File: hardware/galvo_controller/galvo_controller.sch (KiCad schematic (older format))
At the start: 116 parts, among them J1 USB_OTG, J2 Conn_01x03, J3 Conn_01x03, J4 Micro_SD_Card, J5 Red, J6 White, J7 Conn_01x03, J8 Conn_01x03, Q1 DDTD113ZC, Q2 MMBT2222, Q3 MMBT2222, U1 ESP-WROOM-32D, U2 CP2104, U3 TPS54295PWP, U4 PCM3060, U5 NCP1117LP, U6 OPA2134, U7 LME49724, U8 LME49724

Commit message: Working on schematic
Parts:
- J5, J6: footprint (none) -> footprint:RCJ-01x
- Q2, Q3: footprint (none) -> TO_SOT_Packages_SMD:SOT-23; Part (none) -> MMBT2222ALT3GOSCT-ND; Source (none) -> DigiKey
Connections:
- net labels added: LASER
- net labels removed: LASER_EN

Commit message: Working on footprints
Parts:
- L1, L2: footprint (none) -> footprint:CLF7045-D
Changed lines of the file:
@@
 F 0 "L2" V 6700 1700 50  0000 C CNN
 F 1 "2.2u" V 6825 1700 50  0000 C CNN
-F 2 "" H 6750 1700 50  0001 C CNN
+F 2 "footprint:CLF7045-D" H 6750 1700 50  0001 C CNN
 F 3 "" H 6750 1700 50  0001 C CNN
 F 4 "DigiKey" H 6750 1700 60  0001 C CNN "Source"
@@
 F 0 "L1" V 4400 1700 50  0000 C CNN
 F 1 "3.3u" V 4525 1700 50  0000 C CNN
-F 2 "" H 4450 1700 50  0001 C CNN
+F 2 "footprint:CLF7045-D" H 4450 1700 50  0001 C CNN
 F 3 "" H 4450 1700 50  0001 C CNN
 F 4 "DigiKey" H 4450 1700 60  0001 C CNN "Source"

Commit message: Working on footprints
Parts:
- removed J4: Micro_SD_Card, symbol Micro_SD_Card
- added J4: Micro_SD_Card_Det, footprint:503182-1853, symbol Micro_SD_Card_Det
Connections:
- wire segments 399 -> 400
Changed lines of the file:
@@
-$EndComp
-$Comp
-L Micro_SD_Card J4
-U 1 1 5AA9BDBD
-P 10500 9100
-F 0 "J4" H 9850 9700 50  0000 C CNN
-F 1 "Micro_SD_Card" H 11150 9700 50  0000 R CNN
-F 2 "" H 11650 9400 50  0001 C CNN
-F 3 "" H 10500 9100 50  0001 C CNN
-	1    10500 9100
-	1    0    0    -1
 $EndComp
 $Comp
@@
 L GNDD #PWR43
 U 1 1 5AA746B2
-P 9500 9600
-F 0 "#PWR43" H 9500 9350 50  0001 C CNN
-F 1 "GNDD" H 9500 9475 50  0000 C CNN
-F 2 "" H 9500 9600 50  0001 C CNN
-F 3 "" H 9500 9600 50  0001 C CNN
-	1    9500 9600
+P 9500 9800
+F 0 "#PWR43" H 9500 9550 50  0001 C CNN
+F 1 "GNDD" H 9500 9675 50  0000 C CNN
+F 2 "" H 9500 9800 50  0001 C CNN
+F 3 "" H 9500 9800 50  0001 C CNN
+	1    9500 9800
 	1    0    0    -1
 $EndComp
@@
 	9600 9300 9500 9300
 Wire Wire Line
-	9500 9300 9500 9600
+	9500 9300 9500 9800
 $Comp
 L +3.3V #PWR42
@@
 Wire Wire Line
 	8700 8050 8700 8100
+$Comp
+L Micro_SD_Card_Det J4
+U 1 1 5AA55079
+P 10500 9200
+F 0 "J4" H 9850 9900 50  0000 C CNN
+F 1 "Micro_SD_Card_Det" H 11150 9900 50  0000 R CNN
+F 2 "footprint:503182-1853" H 12550 9900 50  0001 C CNN
+F 3 "" H 10500 9300 50  0001 C CNN
+F 4 "DigiKey" H 10500 9200 60  0001 C CNN "Source"
+F 5 "WM9750CT-ND" H 10500 9200 60  0001 C CNN "Part"
+	1    10500 9200
+	1    0    0    -1
+$EndComp
+Wire Wire Line
+	9600 9700 9500 9700
+Connection ~ 9500 9700
 $EndSCHEMATC

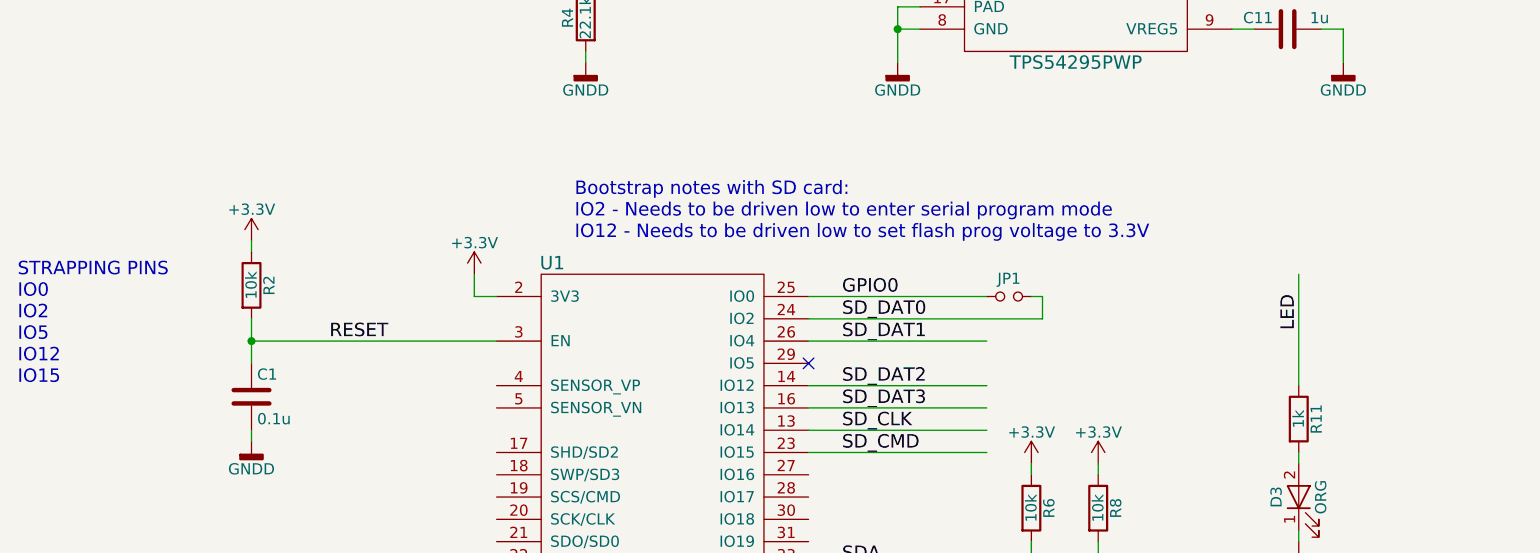
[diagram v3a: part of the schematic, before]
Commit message: Finished BOM, exported to layout
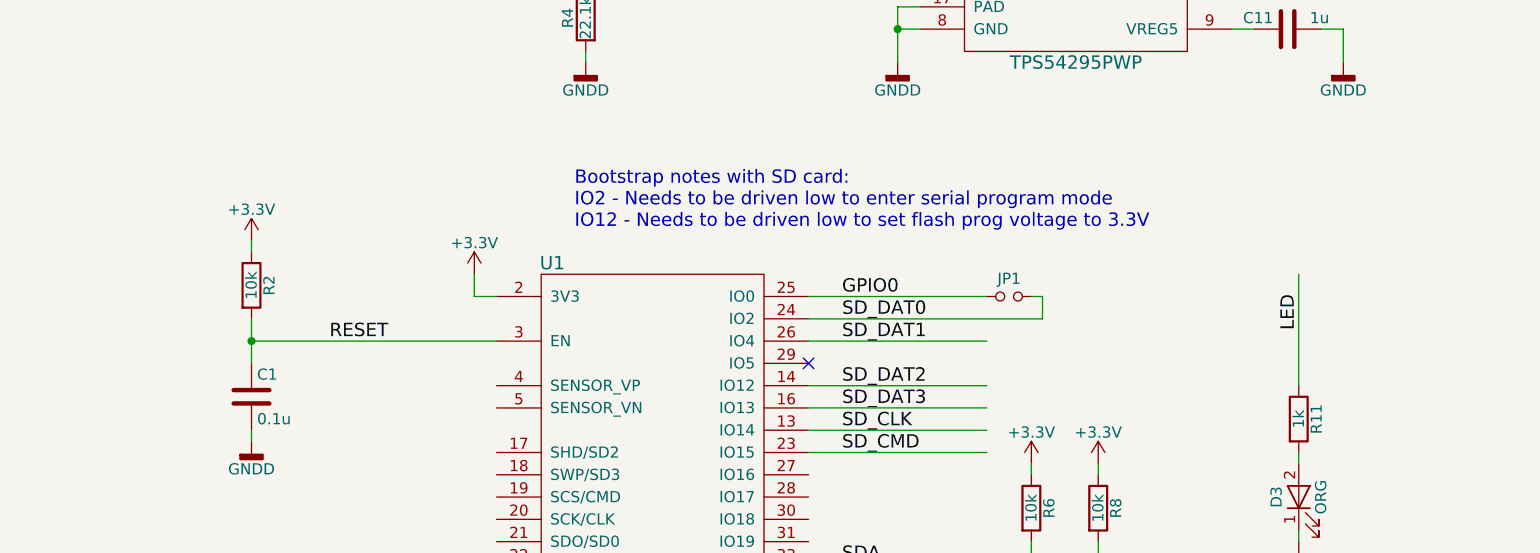
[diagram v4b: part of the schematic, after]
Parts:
- C10, C7: footprint (none) -> Capacitors_SMD:C_0603; Part (none) -> 490-9734-1-ND; Source (none) -> DigiKey
- C11: footprint (none) -> Capacitors_SMD:C_0805; Part (none) -> 490-1691-1-ND; Source (none) -> DigiKey
- C13, C14, C4, C5: Part 311-1995-1-ND -> 490-6509-1-ND
- C28, C29, C30, C31, C32, C33: footprint (none) -> Capacitors_SMD:C_0603; Part (none) -> 490-11460-1-ND; Source (none) -> DigiKey
- C3: footprint (none) -> Capacitors_SMD:C_0805; Part (none) -> 490-5422-1-ND; Source (none) -> DigiKey
- JP1, JP2: Part (none) -> 3M9457-02-ND
- R1: Part (none) -> 311-2.20KHRCT-ND; Source (none) -> DigiKey
- R10, R14, R15, R16, R17, R18, R19, R2, R26, R27, R28, R29, R30, R31, R6, R8, R9: Part (none) -> 311-10.0KHRCT-ND; Source (none) -> DigiKey
- R11, R20, R21, R5, R7: Part (none) -> 311-1.00KHRCT-ND; Source (none) -> DigiKey
- R12: Part (none) -> 311-73.2KHRCT-ND; Source (none) -> DigiKey
- R13, R4: Part (none) -> 311-22.1KHRCT-ND; Source (none) -> DigiKey
- R22, R23, R24, R25: Part (none) -> 311-8.06KHRCT-ND; Source (none) -> DigiKey
- R3: Part (none) -> 311-124KHRCT-ND; Source (none) -> DigiKey
- R32, R33: Part (none) -> 311-20.0KHRCT-ND; Source (none) -> DigiKey
- R34, R35, R36, R37: Part (none) -> 311-0.0GRCT-ND; Source (none) -> DigiKey
- R38, R39: Part (none) -> 311-47.0KHRCT-ND; Source (none) -> DigiKey
- U1: Part (none) -> 1528-1801-ND; Source eBay -> DigiKey
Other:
- note removed: "STRAPPING PINS\nIO0\nIO2\nIO5\nIO12\nIO15"

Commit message: Working on layout
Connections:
- net labels added: D_N, D_P, VBUS, VOUTL_N, VOUTL_P, VOUTR_N, VOUTR_P, X_N, X_P, Y_N, Y_P
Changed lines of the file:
@@
 	9600 9700 9500 9700
 Connection ~ 9500 9700
+Text Label 10100 6550 0    60   ~ 0
+VOUTR_N
+Text Label 10100 6750 0    60   ~ 0
+VOUTR_P
+Text Label 10100 6950 0    60   ~ 0
+VOUTL_N
+Text Label 10100 7150 0    60   ~ 0
+VOUTL_P
+Text Label 14600 5750 0    60   ~ 0
+X_P
+Text Label 14600 5850 0    60   ~ 0
+X_N
+Text Label 14600 7850 0    60   ~ 0
+Y_P
+Text Label 14600 7950 0    60   ~ 0
+Y_N
+Text Label 2150 9000 0    60   ~ 0
+D_N
+Text Label 2150 8900 0    60   ~ 0
+D_P
+Text Label 2150 8800 0    60   ~ 0
+VBUS
 $EndSCHEMATC

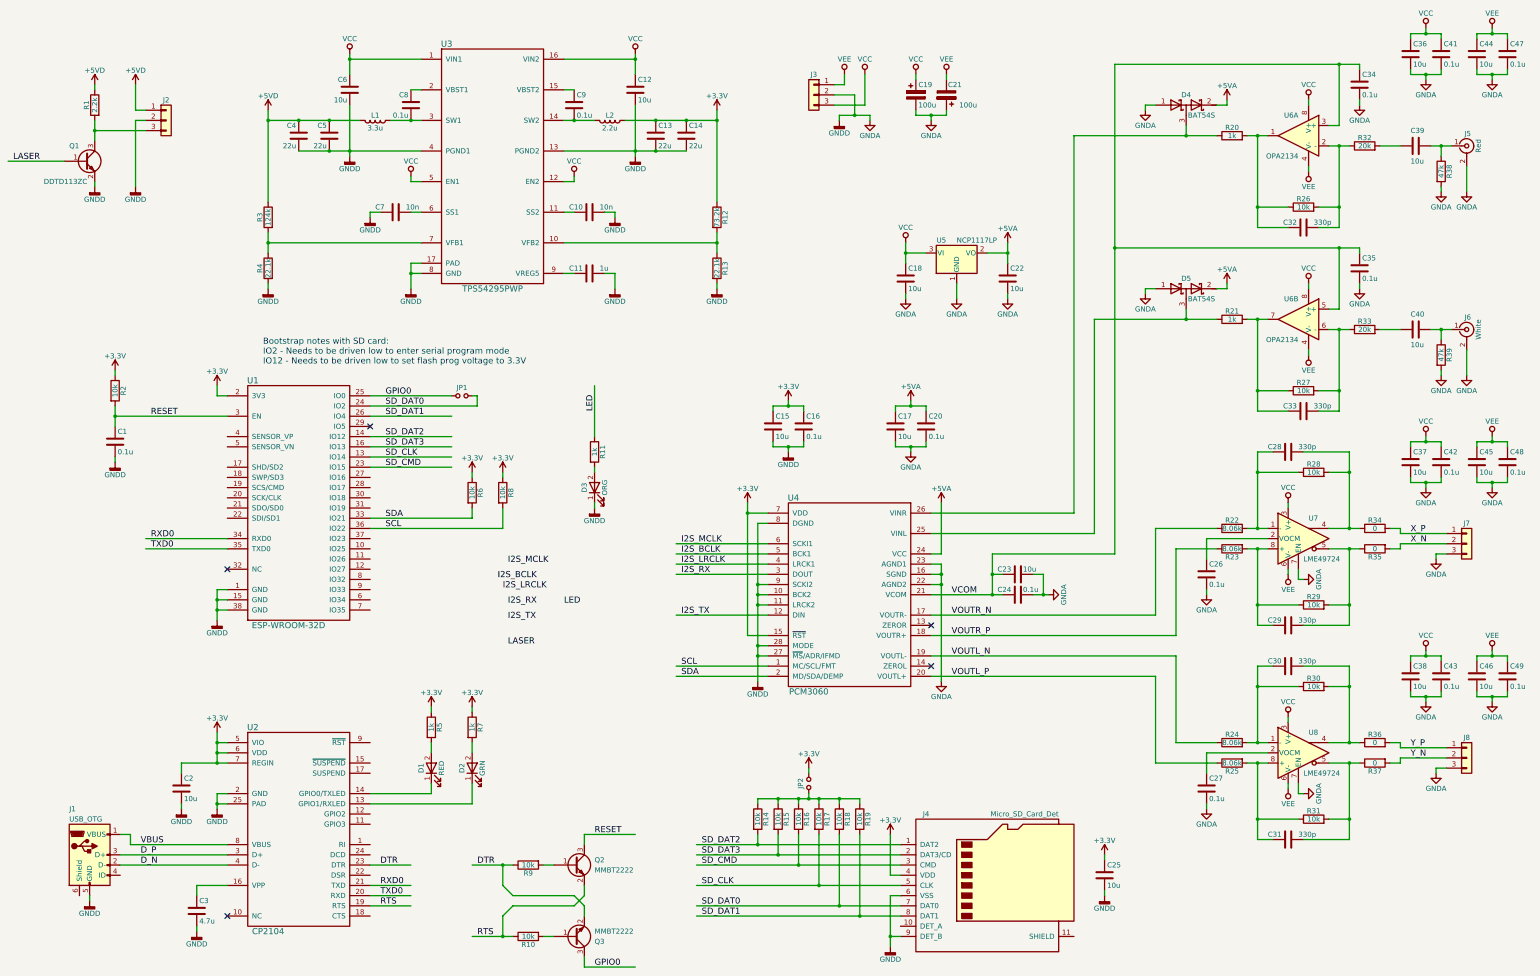
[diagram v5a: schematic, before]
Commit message: Switched to logic buffer for laser enable
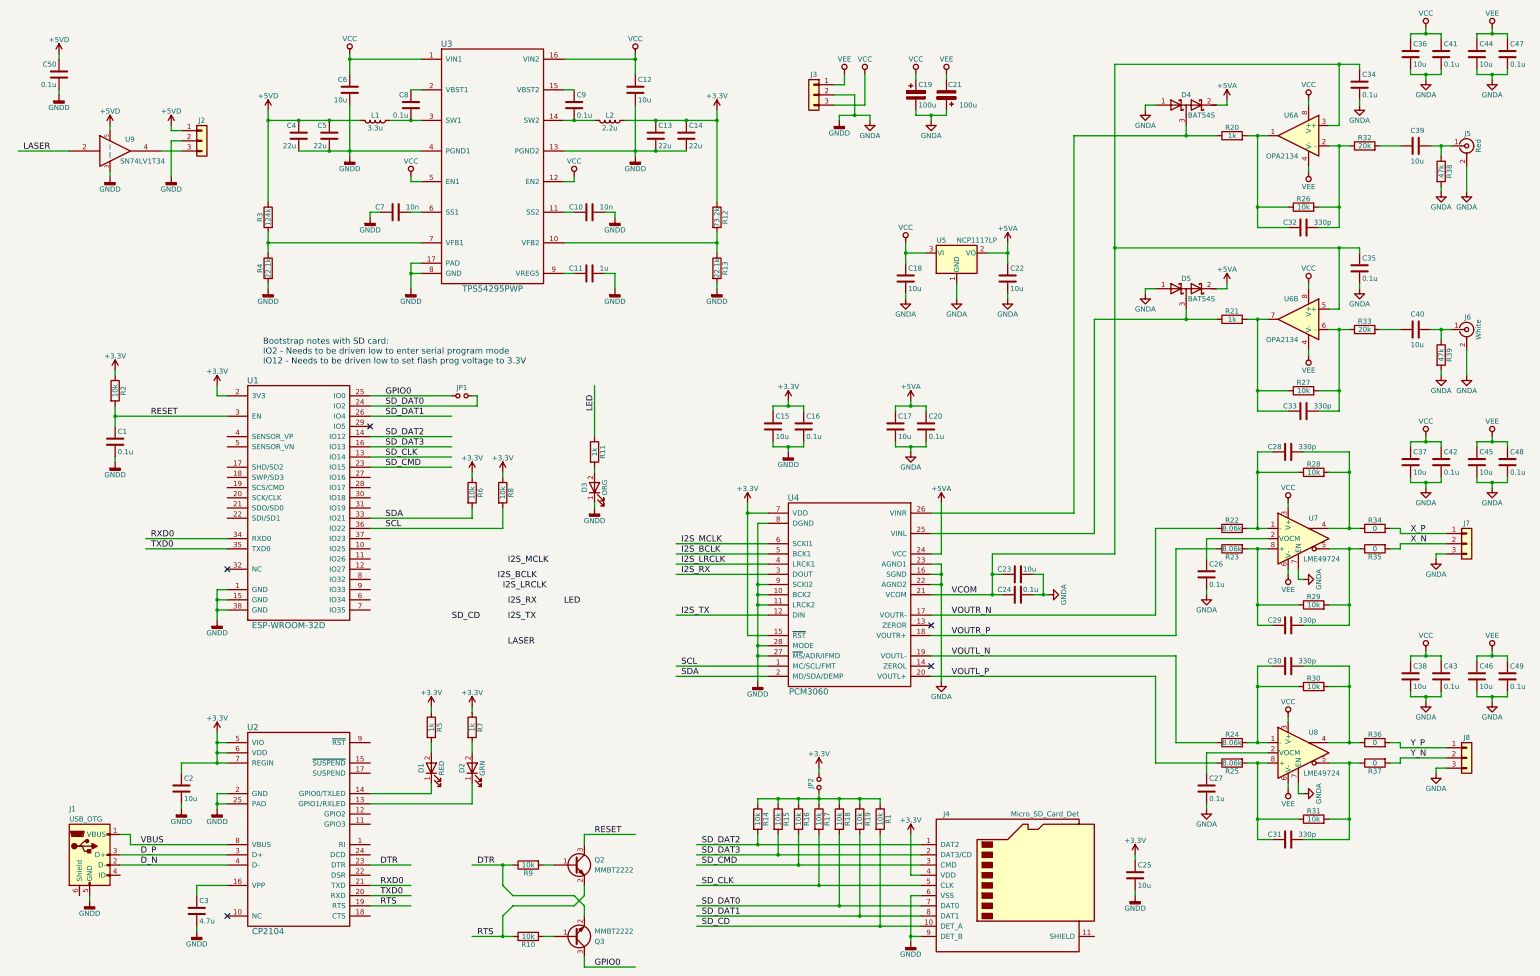
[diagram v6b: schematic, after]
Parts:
- removed Q1: DDTD113ZC, TO_SOT_Packages_SMD:SOT-23, symbol Q_NPN_BEC
- added C50: 0.1u, Capacitors_SMD:C_0603, symbol C
- added U9: SN74LV1T34, TO_SOT_Packages_SMD:SOT-23-5, symbol SN74LV1T34
- R1: value 2.2k -> 10k; Part 311-2.20KHRCT-ND -> 311-10.0KHRCT-ND
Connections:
- net labels added: SD_CD
- wire segments 400 -> 403
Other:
- moved on the sheet: C25, J2, J4, JP2

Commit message: Working on layout
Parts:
- renumbered C50 to C1, C9 to C10, C10 to C11, C11 to C12, C12 to C13, C13 to C14, C14 to C15, C15 to C16, C16 to C17, C17 to C18, C18 to C19, C1 to C2, C19 to C20, C20 to C21, C21 to C22, C22 to C23, C23 to C24, C24 to C25, C25 to C26, C26 to C27, C27 to C28, C28 to C29, C2 to C3, C29 to C30, C30 to C31, C31 to C32, C32 to C33, C33 to C34, C34 to C35, C35 to C36, C36 to C37, C37 to C38, C38 to C39, C3 to C4, C39 to C40, C40 to C41, C41 to C42, C42 to C43, C43 to C44, C44 to C45, C45 to C46, C46 to C47, C47 to C48, C48 to C49, C4 to C5, C49 to C50, C5 to C6, C6 to C7, C7 to C8, C8 to C9, Q2 to Q1, Q3 to Q2, R2 to R1, R11 to R10, R12 to R11, R13 to R12, R14 to R13, R15 to R14, R16 to R15, R17 to R16, R18 to R17, R19 to R18, R1 to R19, R3 to R2, R4 to R3, R5 to R4, R6 to R5, R7 to R6, R8 to R7, R9 to R8, R10 to R9, U9 to U1, U1 to U2, U2 to U3, U3 to U4, U4 to U5, U5 to U6, U6 to U7, U7 to U8, U8 to U9

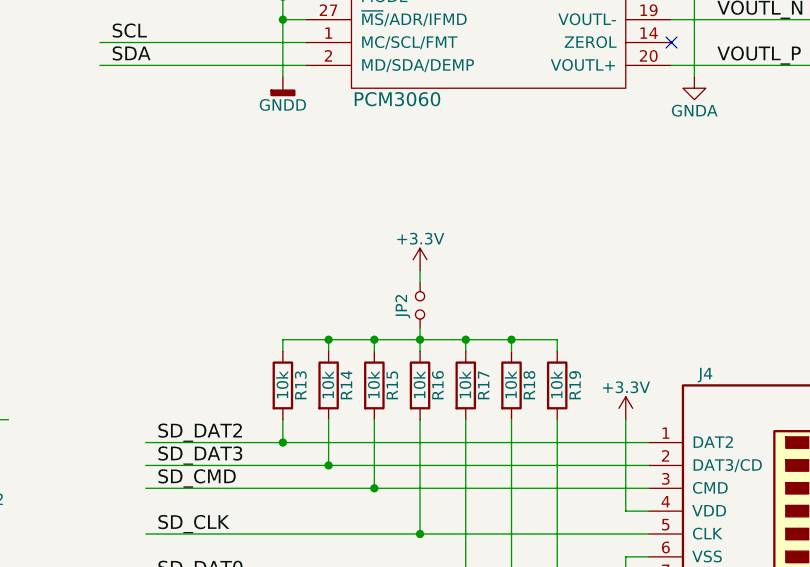
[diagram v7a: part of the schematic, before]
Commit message: Tweaked SD card pullup jumpers
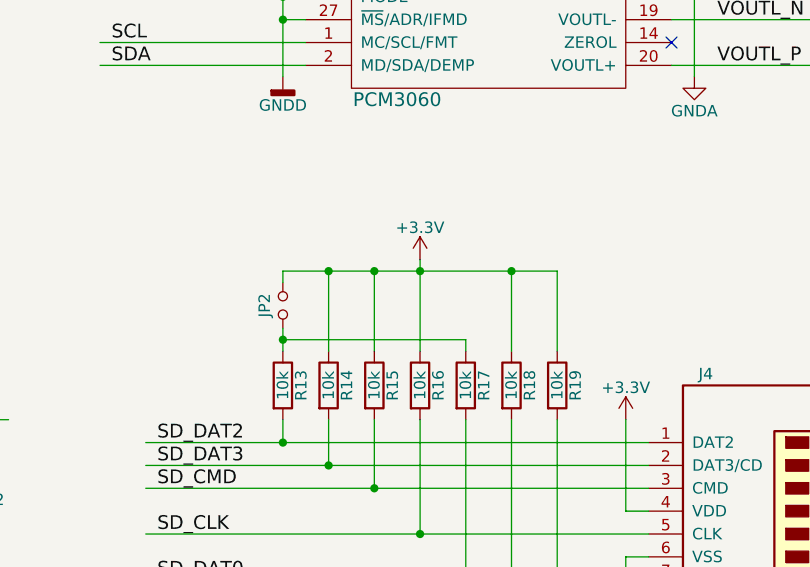
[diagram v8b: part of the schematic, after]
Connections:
- wire segments 403 -> 404
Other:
- moved on the sheet: JP2
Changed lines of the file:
@@
 L +3.3V #PWR39
 U 1 1 5AA8914A
-P 8800 8050
-F 0 "#PWR39" H 8800 7900 50  0001 C CNN
-F 1 "+3.3V" H 8800 8190 50  0000 C CNN
-F 2 "" H 8800 8050 50  0001 C CNN
-F 3 "" H 8800 8050 50  0001 C CNN
-	1    8800 8050
+P 8800 8000
+F 0 "#PWR39" H 8800 7850 50  0001 C CNN
+F 1 "+3.3V" H 8800 8140 50  0000 C CNN
+F 2 "" H 8800 8000 50  0001 C CNN
+F 3 "" H 8800 8000 50  0001 C CNN
+	1    8800 8000
 	1    0    0    -1
 $EndComp
@@
 L Jumper_NO_Small JP2
 U 1 1 5AA977C1
-P 8800 8200
-F 0 "JP2" H 8800 8280 50  0000 C CNN
-F 1 "Jumper_NO_Small" H 8810 8140 50  0001 C CNN
-F 2 "Pin_Headers:Pin_Header_Straight_1x02_Pitch2.54mm" H 8800 8200 50  0001 C CNN
-F 3 "" H 8800 8200 50  0001 C CNN
-F 4 "DigiKey" H 8800 8200 60  0001 C CNN "Source"
-F 5 "3M9457-02-ND" H 8800 8200 60  0001 C CNN "Part"
-	1    8800 8200
+P 8200 8200
+F 0 "JP2" H 8200 8280 50  0000 C CNN
+F 1 "Jumper_NO_Small" H 8210 8140 50  0001 C CNN
+F 2 "Pin_Headers:Pin_Header_Straight_1x02_Pitch2.54mm" H 8200 8200 50  0001 C CNN
+F 3 "" H 8200 8200 50  0001 C CNN
+F 4 "DigiKey" H 8200 8200 60  0001 C CNN "Source"
+F 5 "3M9457-02-ND" H 8200 8200 60  0001 C CNN "Part"
+	1    8200 8200
 	0    -1   -1   0
 $EndComp
@@
 Wire Wire Line
 	7600 9600 9800 9600
-Connection ~ 9200 8350
-Wire Wire Line
-	9400 8350 9400 8400
+Wire Wire Line
+	9400 8050 9400 8400
 Wire Wire Line
 	1350 1100 1350 1050
@@
 Wire Wire Line
 	9800 9700 9700 9700
-Wire Wire Line
-	8800 8050 8800 8100
-Connection ~ 8400 8350
-Wire Wire Line
-	8400 8400 8400 8350
-Connection ~ 8600 8350
-Wire Wire Line
-	8600 8400 8600 8350
-Connection ~ 8800 8350
-Wire Wire Line
-	8800 8300 8800 8400
-Connection ~ 9000 8350
-Wire Wire Line
-	9000 8400 9000 8350
-Wire Wire Line
-	9200 8350 9200 8400
-Wire Wire Line
-	8200 8350 9400 8350
-Wire Wire Line
-	8200 8400 8200 8350
 Connection ~ 8200 8800
 Wire Wire Line
@@
 Wire Wire Line
 	1900 4200 1900 4150
+Wire Wire Line
+	8200 8400 8200 8300
+Wire Wire Line
+	8200 8350 9000 8350
+Wire Wire Line
+	9000 8350 9000 8400
+Connection ~ 8200 8350
+Wire Wire Line
+	8200 8100 8200 8050
+Wire Wire Line
+	8200 8050 9400 8050
+Wire Wire Line
+	9200 8400 9200 8050
+Connection ~ 9200 8050
+Wire Wire Line
+	8800 8000 8800 8400
+Connection ~ 8800 8050
+Wire Wire Line
+	8600 8400 8600 8050
+Connection ~ 8600 8050
+Wire Wire Line
+	8400 8400 8400 8050
+Connection ~ 8400 8050
 $EndSCHEMATC
